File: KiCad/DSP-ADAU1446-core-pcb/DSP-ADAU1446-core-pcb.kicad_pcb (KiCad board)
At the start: 4 copper layers, 83 parts, among them IC1 24AA256, J1 POW_CONN, P1 RCA, P2 CONN_02x05, P3 CONN_02x05, P4 CONN_02x05, P5 CONN_02X05, P6 CONN_02x05, P7 CONN_02x05, Q1 12.288MHz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

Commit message: - pcb development update
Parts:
- Q2: value NJT4030P -> FMMT734; footprint TO_SOT_Packages_SMD:SOT-223-3Lead_TabPin2 -> w_smd_trans:sot23
- moved JP1 120.5 mm to (107.6, 128.7), turned to 90 degrees
- moved R5 118.6 mm to (110.9, 128.6), turned to 180 degrees
- moved C18 40.2 mm to (110.5, 135.2)
- moved P6 30.0 mm to (165.4, 116.5)
- moved R18 30.0 mm to (161.4, 116.5)
- moved R19 30.0 mm to (161.4, 114.4)
- moved R17 30.0 mm to (161.4, 118.5)
- moved R25 30.0 mm to (161.4, 120.5)
- moved C9 15.2 mm to (121.5, 136.2), turned to 180 degrees
- moved C10 13.8 mm to (106.0, 116.1), turned to 0 degrees
- moved R1 12.5 mm to (109.4, 144.6)
- moved R4 12.4 mm to (105.0, 147.5)
- moved Q1 12.4 mm to (107.5, 147.5)
- moved C2 12.4 mm to (107.1, 145.4)
- moved R7 12.0 mm to (114.1, 128.7), turned to 180 degrees
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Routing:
- net GND: track 12.1 -> 91.0 mm, vias 0 -> 24
- net VAA: track 37.8 -> 3.78 mm, vias 2 -> 0
- net VDD: track 15.9 -> 43.3 mm, vias 3 -> 11
- net /ADAU1446/PVDD: track 2.04 -> 14.7 mm
- net Net-(C3-Pad1): track 9.29 -> 19.8 mm, vias 0 -> 5
- net Net-(JP1-Pad1): track 0.00 -> 10.4 mm
- net (no net): track 7.42 -> 0.00 mm, vias 6 -> 0
- net SCL/CCLK: track 0.00 -> 6.82 mm
- net Net-(C2-Pad1): track 0.54 -> 5.43 mm
- net SDA/COUT: track 0.00 -> 4.63 mm
- net ~RESET: track 7.59 -> 5.34 mm
- net Net-(R6-Pad1): track 0.00 -> 2.02 mm
- net Net-(Q1-Pad3): track 1.88 -> 0.05 mm
- net Net-(C23-Pad2): track 0.00 -> 1.49 mm
- net Net-(R10-Pad1): track 0.00 -> 1.47 mm
- removed copper zone on F.Cu, net Net-(C2-Pad1)
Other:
- rule trace_min: 0.127 -> 0.152
- rule via_min_size: 0.5 -> 0.6

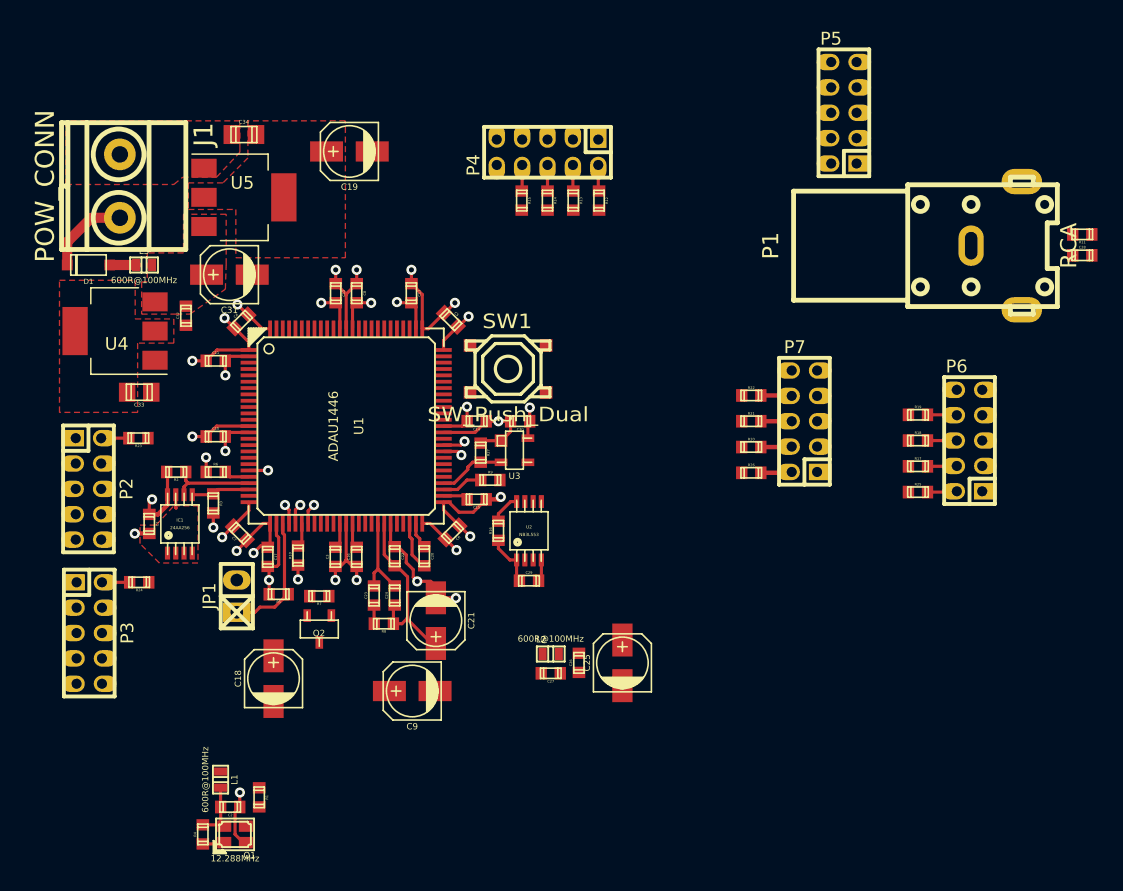
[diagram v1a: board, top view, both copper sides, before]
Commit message: -pcb update - changed footprint of IC1 and U2 to SO8
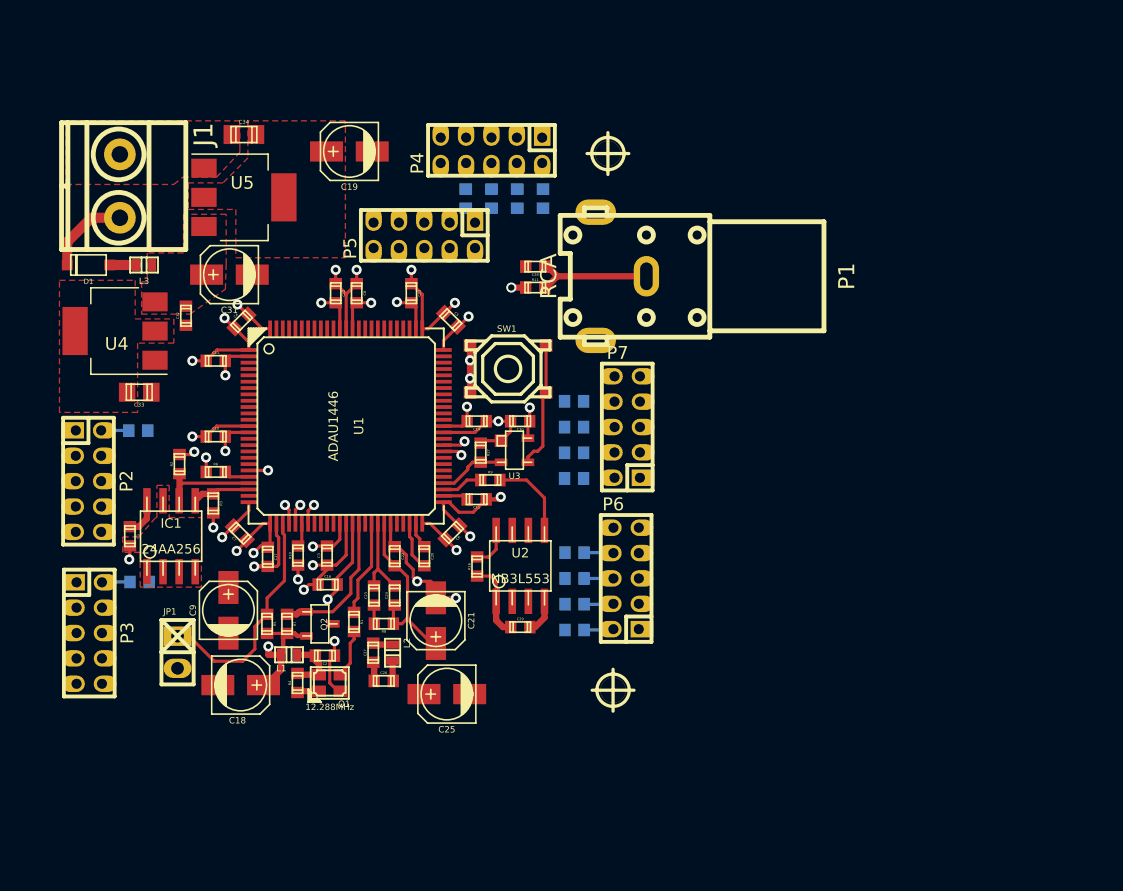
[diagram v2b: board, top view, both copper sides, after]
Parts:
- added G***: LOGO, w_logo:Logo_silk_OSHW_6x6mm, B.Cu at (128.1, 133.1)
- added hole_2mm: VAL**, w_details:hole_2mm, F.Cu at (137.3, 136.1)
- added hole_2mm: VAL**, w_details:hole_2mm, F.Cu at (136.9, 93.8)
- IC1, U2: footprint w_smd_dil:msoic-8 -> w_smd_dil:so-8
- R12, R13, R14, R15, R17, R18, R19, R20, R21, R22, R23, R24, R25, R26: moved to B.Cu
- moved R11 43.3 mm to (131.2, 104.4), turned to 0 degrees
- moved C28 43.1 mm to (131.2, 102.7), turned to 180 degrees
- moved P5 34.5 mm to (122.4, 100.3), turned to 180 degrees
- moved R25 29.2 mm to (134.3, 131.4)
- moved R17 29.2 mm to (134.3, 129.4)
- moved R18 29.2 mm to (134.3, 127.3)
- moved R19 29.2 mm to (134.3, 125.3)
- moved P6 29.2 mm to (138.3, 127.3)
- moved P1 25.7 mm to (139.9, 103.5), turned to 90 degrees
- moved C9 15.8 mm to (107.0, 129.8), turned to 90 degrees
- moved R1 15.7 mm to (116.9, 130.8)
- moved C26 15.5 mm to (119.2, 135.4), turned to 0 degrees
- moved C27 14.1 mm to (118.4, 133.2), turned to 90 degrees
- moved Q1 14.1 mm to (115.0, 135.6)
- moved R4 14.1 mm to (112.4, 135.6)
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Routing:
- net VDD: track 43.3 -> 58.8 mm, vias 11 -> 13
- net Net-(Q2-Pad1): track 0.00 -> 11.5 mm
- net ~BRD_RST: track 0.00 -> 9.99 mm
- net Net-(C28-Pad2): track 0.00 -> 9.68 mm
- net Net-(JP1-Pad1): track 10.4 -> 18.2 mm
- net GND: track 91.0 -> 98.7 mm, vias 24 -> 27
- net /ADAU1446/XTALI: track 0.00 -> 7.59 mm
- net CLKOUT: track 0.00 -> 6.66 mm
- net Net-(Q1-Pad3): track 0.05 -> 3.91 mm
- net Net-(P7-Pad6): track 2.44 -> 0.00 mm
- net Net-(P7-Pad8): track 2.45 -> 0.05 mm
- net Net-(P7-Pad4): track 2.45 -> 0.05 mm
- net /CONN/MCLKD1: track 2.47 -> 0.09 mm
- net Net-(P4-Pad2): track 2.08 -> 0.00 mm
- net SCL/CCLK: track 6.82 -> 8.89 mm
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
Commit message: finished schematic and PCB for v0.1
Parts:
- removed the G*** at (128.1, 133.1)
- removed hole_2mm (x2): VAL**, w_details:hole_2mm
- added G***: LOGO, w_logo:Logo_silk_OSHW_12x13mm, B.Cu at (106.6, 97.5)
- added hole_2mm5: VAL**, w_details:hole_2mm5, F.Cu at (99.9, 136.7)
- added hole_2mm5: VAL**, w_details:hole_2mm5, F.Cu at (129.2, 97.9)
- added hole_2mm5: VAL**, w_details:hole_2mm5, F.Cu at (132.0, 136.5)
- P1: value RCA -> CONN_01X02; footprint w_conn_av:rca_yellow -> Socket_Strips:Socket_Strip_Straight_1x02_Pitch2.54mm
- SW1: value SW_Push_Dual -> ALPS_switch; footprint w_switch:smd_push2 -> w_switch:smd_push_ALPS
- moved P4 37.2 mm to (138.6, 129.1), turned to 90 degrees
- moved R15 36.9 mm to (134.7, 133.1), turned to 180 degrees
- moved R14 34.5 mm to (134.7, 131.2), turned to 180 degrees
- moved P6 34.2 mm to (134.1, 93.4), turned to 180 degrees
- moved R25 34.2 mm to (138.2, 97.4), turned to 90 degrees
- moved R13 32.2 mm to (134.7, 129.2), turned to 180 degrees
- moved R17 32.0 mm to (136.1, 97.4), turned to 90 degrees
- moved R18 29.9 mm to (134.1, 97.4), turned to 90 degrees
- moved R12 29.9 mm to (134.7, 127.2), turned to 180 degrees
- moved R19 28.0 mm to (132.1, 97.4), turned to 90 degrees
- moved P7 27.6 mm to (121.7, 93.4), turned to 180 degrees
- moved R26 23.5 mm to (125.7, 97.5), turned to 90 degrees
- moved R20 22.5 mm to (123.7, 97.5), turned to 90 degrees
- moved R21 21.8 mm to (121.8, 97.5), turned to 90 degrees
- moved R22 21.5 mm to (119.7, 97.5), turned to 90 degrees
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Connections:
- P2 pad 4: LRCLK0 -> SDATA_IN0
- P2 pad 8: SDATA_IN0 -> LRCLK0
- P3 pad 4: LRCLK1 -> SDATA_IN1
- P3 pad 8: SDATA_IN1 -> LRCLK1
- R12 pad 2: Net-(P4-Pad2) -> Net-(P4-Pad8)
- R13 pad 2: Net-(P4-Pad4) -> Net-(P4-Pad6)
- R14 pad 2: Net-(P4-Pad6) -> Net-(P4-Pad4)
- R15 pad 2: Net-(P4-Pad8) -> Net-(P4-Pad2)
- SW1 pad 2: ~BRD_RST -> GND
- SW1 pad 3: GND -> ~BRD_RST
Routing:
- net Net-(C3-Pad1): track 21.4 -> 113.1 mm, vias 6 -> 8
- net GND: track 98.7 -> 159.2 mm, vias 27 -> 53
- net VAA: track 3.78 -> 46.9 mm, vias 0 -> 8
- net Net-(R24-Pad2): track 0.00 -> 43.0 mm, vias 0 -> 1
- net SCL/CCLK: track 8.89 -> 50.7 mm, vias 0 -> 2
- net SDA/COUT: track 4.69 -> 45.0 mm, vias 0 -> 2
- net VDD: track 58.8 -> 96.3 mm, vias 13 -> 29
- net LRCLK2: track 0.00 -> 35.8 mm, vias 0 -> 1
- net BCLK2: track 0.00 -> 33.7 mm, vias 0 -> 1
- net BCLK0: track 0.00 -> 33.7 mm, vias 0 -> 3
- net Net-(R23-Pad2): track 0.00 -> 32.7 mm, vias 0 -> 1
- net Net-(R25-Pad2): track 0.00 -> 32.5 mm, vias 0 -> 1
- net MP4: track 0.00 -> 30.9 mm, vias 0 -> 3
- net SDATA_OUT0: track 0.00 -> 30.6 mm, vias 0 -> 3
- net MP5: track 0.00 -> 28.6 mm, vias 0 -> 3
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- added copper zone on B.Cu, net GND
- added copper zone on POW.Cu, net GND
- added copper zone on POW.Cu, net VAA
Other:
- net class Default: clearance 0.2 -> 0.1524; via_drill 0.5 -> 0.4
- rule trace_clearance: 0.2 -> 0.1524
- rule trace_min: 0.152 -> 0.155
- board text added: "ADAU144x DSP Core by Bogdan T. v0.1"
- board text added: "GPIO"
- board text added: "I2S IN"
- board text added: "I2S OUT"
- board text added: "PROG"

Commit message: Updated schematic and PCB to use SDATA_OUT4 and SDATA_OUT8 with LRCLK4,LRCLK8 and BCLK8,BCLK8
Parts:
- removed G***: LOGO, w_logo:Logo_silk_OSHW_12x13mm
- removed hole_2mm5 (x3): VAL**, w_details:hole_2mm5
- moved P6 12.4 mm to (121.7, 93.5)
- moved R18 12.4 mm to (121.7, 97.5)
- moved R17 12.4 mm to (123.7, 97.5)
- moved R19 12.4 mm to (119.6, 97.5)
- moved R20 12.4 mm to (136.1, 97.7)
- moved R21 12.4 mm to (134.1, 97.7)
- moved R22 12.4 mm to (132.1, 97.7)
- moved P7 12.2 mm to (134.0, 93.5)
- moved R25 0.33 mm to (138.1, 97.7)
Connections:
- P6 pad 2: /CONN/MCLKD0 -> /CONN/MCLKD1
- P7 pad 2: /CONN/MCLKD1 -> /CONN/MCLKD0
- R17 pad 2: LRCLK2 -> SDATA_OUT4
- R18 pad 2: BCLK2 -> BCLK4
- R19 pad 2: SDATA_OUT0 -> LRCLK4
- R20 pad 2: LRCLK3 -> SDATA_OUT8
- R21 pad 2: BCLK3 -> BCLK8
- R22 pad 2: SDATA_OUT1 -> LRCLK8
- U1 pad 3: BCLK3 -> (no net)
- U1 pad 4: LRCLK3 -> (no net)
- U1 pad 6: BCLK2 -> (no net)
- U1 pad 61: (no net) -> SDATA_OUT8
- U1 pad 7: LRCLK2 -> (no net)
- U1 pad 74: (no net) -> BCLK8
- U1 pad 78: (no net) -> LRCLK8
- U1 pad 79: (no net) -> SDATA_OUT4
- U1 pad 94: SDATA_OUT1 -> (no net)
- U1 pad 96: (no net) -> BCLK4
- U1 pad 97: (no net) -> LRCLK4
- U1 pad 98: SDATA_OUT0 -> (no net)
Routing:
- net LRCLK2: track 35.8 -> 0.00 mm, vias 1 -> 0
- net BCLK2: track 33.7 -> 0.00 mm, vias 1 -> 0
- net SDATA_OUT0: track 30.6 -> 0.00 mm, vias 3 -> 0
- net SDATA_OUT8: track 0.00 -> 26.6 mm, vias 0 -> 1
- net BCLK3: track 25.7 -> 0.00 mm, vias 1 -> 0
- net LRCLK3: track 25.4 -> 0.00 mm, vias 1 -> 0
- net LRCLK8: track 0.00 -> 19.1 mm, vias 0 -> 1
- net SDATA_OUT1: track 18.8 -> 0.00 mm, vias 1 -> 0
- net BCLK8: track 0.00 -> 16.6 mm, vias 0 -> 1
- net SDATA_OUT4: track 0.00 -> 16.2 mm, vias 0 -> 1
- net BCLK4: track 0.00 -> 16.0 mm, vias 0 -> 1
- net LRCLK4: track 0.00 -> 14.8 mm, vias 0 -> 1
- net Net-(R26-Pad2): track 26.8 -> 30.5 mm
- net Net-(R25-Pad2): track 32.5 -> 28.8 mm
- net SCL/CCLK: track 50.7 -> 51.9 mm
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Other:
- board text added: "ADAU144x DSP Core by Bogdan T. v0.2"
- board text removed: "ADAU144x DSP Core by Bogdan T. v0.1"
